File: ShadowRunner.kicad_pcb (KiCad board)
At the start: 2 copper layers, 69 parts, among them J1 micro JST SH, J2 GRPB052VWQS-RC, J3 SIM_Card, J4 MM8130-2600, J5 U.FL-R-SMT-1, Q1 DMN65D8L, Q2 DMN65D8L, U1 LM1117-ADJ, U2 USB-C, U3 LM1117-ADJ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

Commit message: All connections made
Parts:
- removed AE2: Antenna_Chip, MyLibs:PCS.06.A
- added J6: PCS.06.A, MyLibs:PCS.06.A, F.Cu at (134.2, 101.4)
- D5: value DIODE -> PMEG2020EPK,315; footprint Diode_SMD:D_0402_1005Metric -> MyLibs:D_0603_1608Metric_Pad1.05x0.95mm_HandSolder
- moved D4 52.5 mm to (152.3, 130.1), turned to 270 degrees
- moved R50 51.7 mm to (151.2, 130.1)
- moved U2 49.7 mm to (153.2, 127.5)
- moved R5 48.9 mm to (151.8, 125.1), turned to 180 degrees
- moved R6 45.0 mm to (151.8, 126.2), turned to 180 degrees
- moved D5 44.2 mm to (151.3, 127.9), turned to 180 degrees
- moved C1 42.5 mm to (141.0, 131.5), turned to 270 degrees
- moved R7 40.3 mm to (139.7, 131.5), turned to 90 degrees
- moved C3 38.1 mm to (138.5, 131.5), turned to 270 degrees
- moved J3 37.5 mm to (112.5, 128.8), turned to 270 degrees
- moved R1 35.9 mm to (137.2, 131.5), turned to 270 degrees
- moved U1 34.0 mm to (138.4, 126.0), turned to 90 degrees
- moved R2 33.8 mm to (135.9, 131.5), turned to 270 degrees
- moved C9 24.6 mm to (147.3, 117.3), turned to 270 degrees
- moved C10 23.9 mm to (148.4, 117.3), turned to 270 degrees
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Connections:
- C16 pad 2: +3V3 -> +1V8
- L5 pad 2: +3V3 -> +1V8
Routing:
- net VBUS: track 31.6 -> 79.8 mm, vias 1 -> 5
- net Net-(R16-Pad2): track 24.0 -> 59.5 mm, vias 2 -> 3
- net GND: track 46.7 -> 79.6 mm, vias 1 -> 32
- net Net-(R15-Pad2): track 35.3 -> 65.4 mm, vias 2 -> 3
- net +3V3: track 88.0 -> 58.0 mm, vias 4 -> 7
- net Net-(D1-Pad1): track 2.24 -> 24.1 mm, vias 0 -> 2
- net GPS_EN: track 7.95 -> 29.2 mm
- net +1V8: track 124.4 -> 108.6 mm, vias 4 -> 8
- net Net-(D2-Pad1): track 6.15 -> 17.5 mm, vias 0 -> 2
- net Net-(R22-Pad2): track 18.3 -> 28.1 mm, vias 0 -> 2
- net ACC_INT2: track 24.3 -> 33.9 mm, vias 0 -> 2
- net Net-(R6-Pad1): track 1.34 -> 10.6 mm, vias 0 -> 1
- net Net-(R11-Pad2): track 51.5 -> 43.5 mm
- net ACC_INT1: track 26.3 -> 34.2 mm
- net ACC_CLK: track 25.1 -> 32.9 mm, vias 0 -> 2
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- added copper zone on In1.Cu, net GND
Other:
- copper layers 2 -> 4
- rule trace_min: 0.2 -> 0.1524
- rule via_min_drill: 0.3 -> 0.24892
- rule via_min_size: 0.4 -> 0.3048

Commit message: Final review
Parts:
- removed AE1: ACAG0301-1575-T, MyLibs:ACAG0301-1575-T
- added U10: ACAG-0301-1575-T, MyLibs:ACAG0301-1575-T, F.Cu at (155.3, 116.1)
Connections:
- J6 pad 1: GND -> Net-(J6-Pad1)
- J6 pad 2: GND -> Net-(J6-Pad2)
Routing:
- net GND: track 79.6 -> 163.7 mm, vias 32 -> 72
- net VBUS: track 79.8 -> 30.8 mm
- net Net-(R22-Pad2): track 28.1 -> 33.5 mm
- net Net-(L1-Pad2): track 7.91 -> 10.5 mm
- net SIM_1V8: track 25.8 -> 27.6 mm
- net +1V8: track 108.6 -> 107.1 mm
- net SIM_CLK: track 7.42 -> 8.90 mm
- net Net-(R16-Pad2): track 59.5 -> 60.7 mm
- net Net-(R15-Pad2): track 65.4 -> 66.5 mm
- net Net-(R3-Pad2): track 5.68 -> 6.61 mm
- net SIM_RST: track 9.44 -> 8.72 mm
- net Net-(J3-PadC2): track 25.5 -> 26.2 mm
- net ACC_MISO: track 31.5 -> 30.9 mm
- net Net-(J3-PadC7): track 28.2 -> 28.7 mm
- net ACC_MOSI: track 30.6 -> 30.7 mm, vias 3 -> 2
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- added copper zone on B.Cu, net GND
- added copper zone on F.Cu, net GND
- added copper zone on In2.Cu, net VBUS

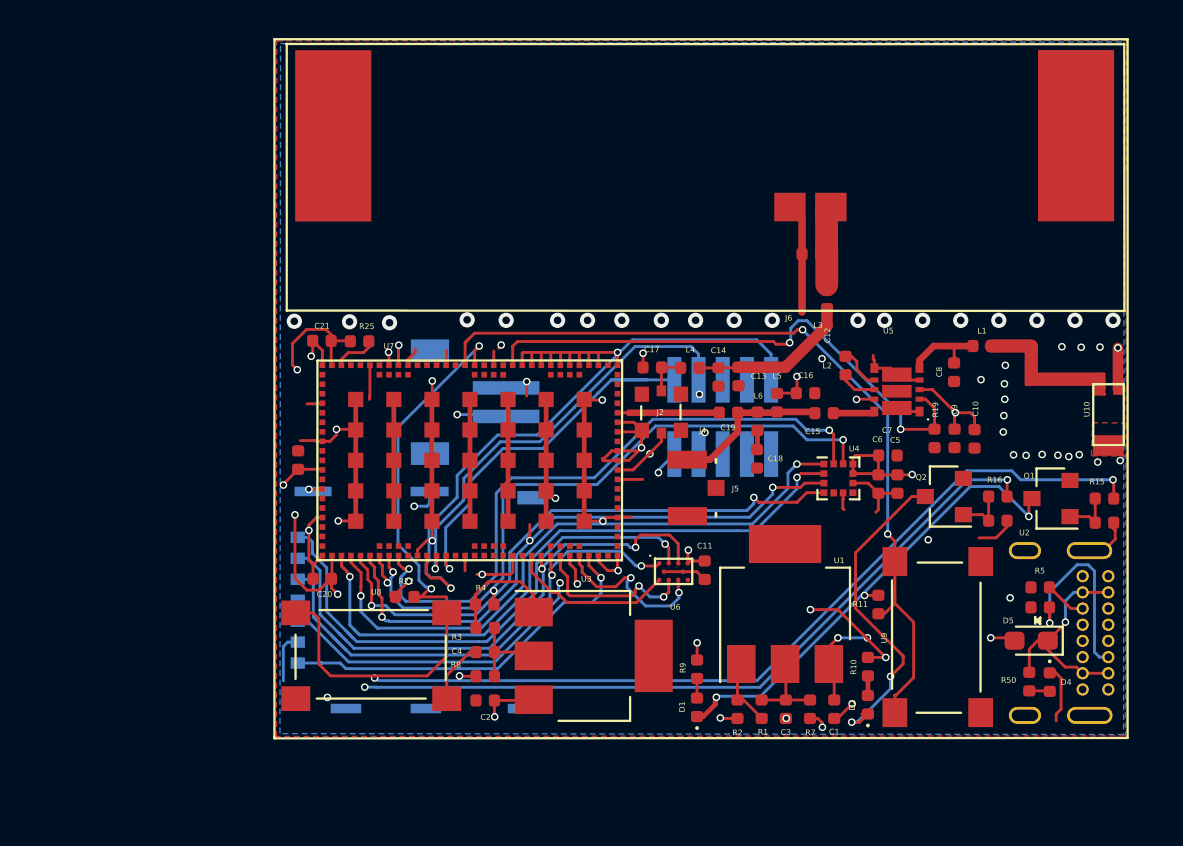
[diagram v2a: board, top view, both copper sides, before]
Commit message: Fixed capacitor footprints
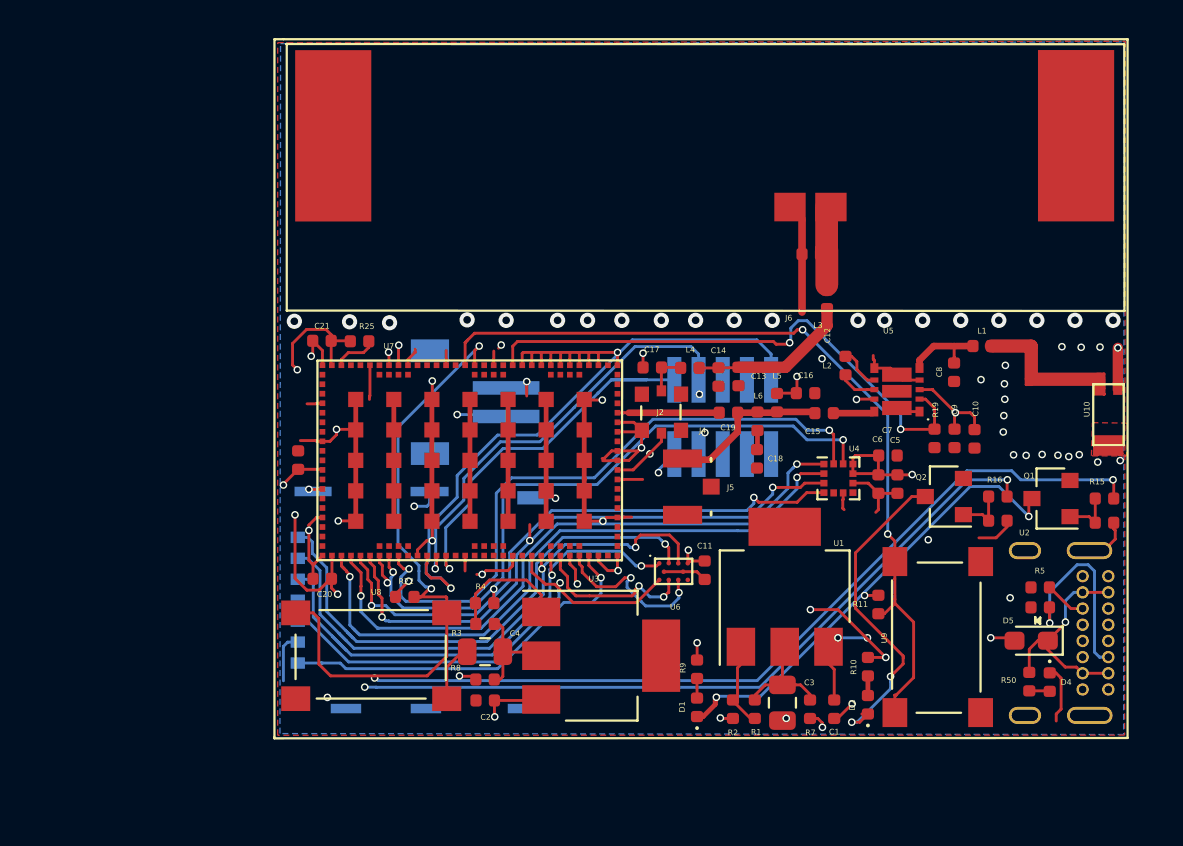
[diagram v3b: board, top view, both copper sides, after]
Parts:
- C12: value 3.5pF -> 6.8pF
- C3, C4: footprint Capacitor_SMD:C_0402_1005Metric -> Capacitor_SMD:C_0805_2012Metric
- L3: value 22nH -> 6.8nH
- moved U1 0.91 mm to (138.4, 125.1)
- moved U3 0.39 mm to (128.8, 128.7)
- moved C3 0.38 mm to (138.3, 131.2)
- moved R1 0.36 mm to (136.8, 131.5)
- moved J5 0.26 mm to (134.5, 119.8)
- moved R2 0.24 mm to (135.7, 131.5)
- moved R3 0.21 mm to (122.7, 127.0)
- moved R8 0.17 mm to (122.7, 130.0)
- moved R4 0.07 mm to (122.6, 126.0)
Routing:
- net Net-(C3-Pad1): track 4.45 -> 6.07 mm
- net Net-(C4-Pad1): track 4.69 -> 5.74 mm
- net GND: track 163.7 -> 163.0 mm
